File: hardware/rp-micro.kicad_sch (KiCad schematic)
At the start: 43 parts, among them J1 USB_C_Receptacle_USB2.0, J2 Conn_01x12, J3 Conn_01x12, J4 Conn_01x05, SW1 BOOT, SW2 RESET, U1 RT9013-33GB, U2 W25Q64JVXGIQ, U3 RP2040, Y1 12MHz

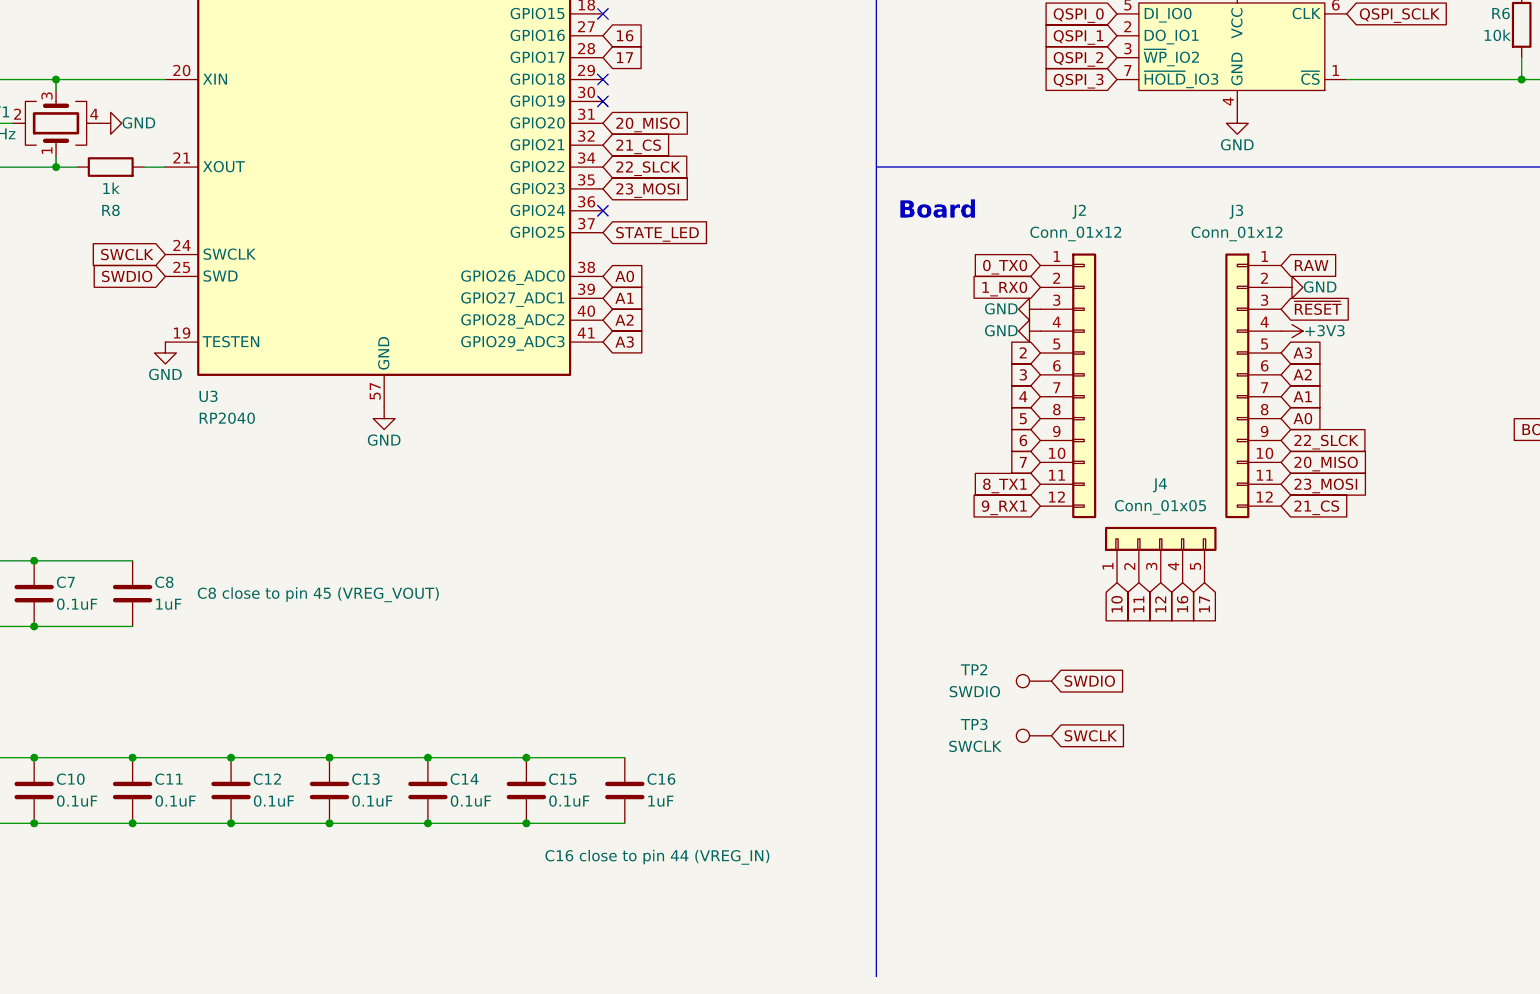
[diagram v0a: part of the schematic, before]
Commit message: Fix the typo
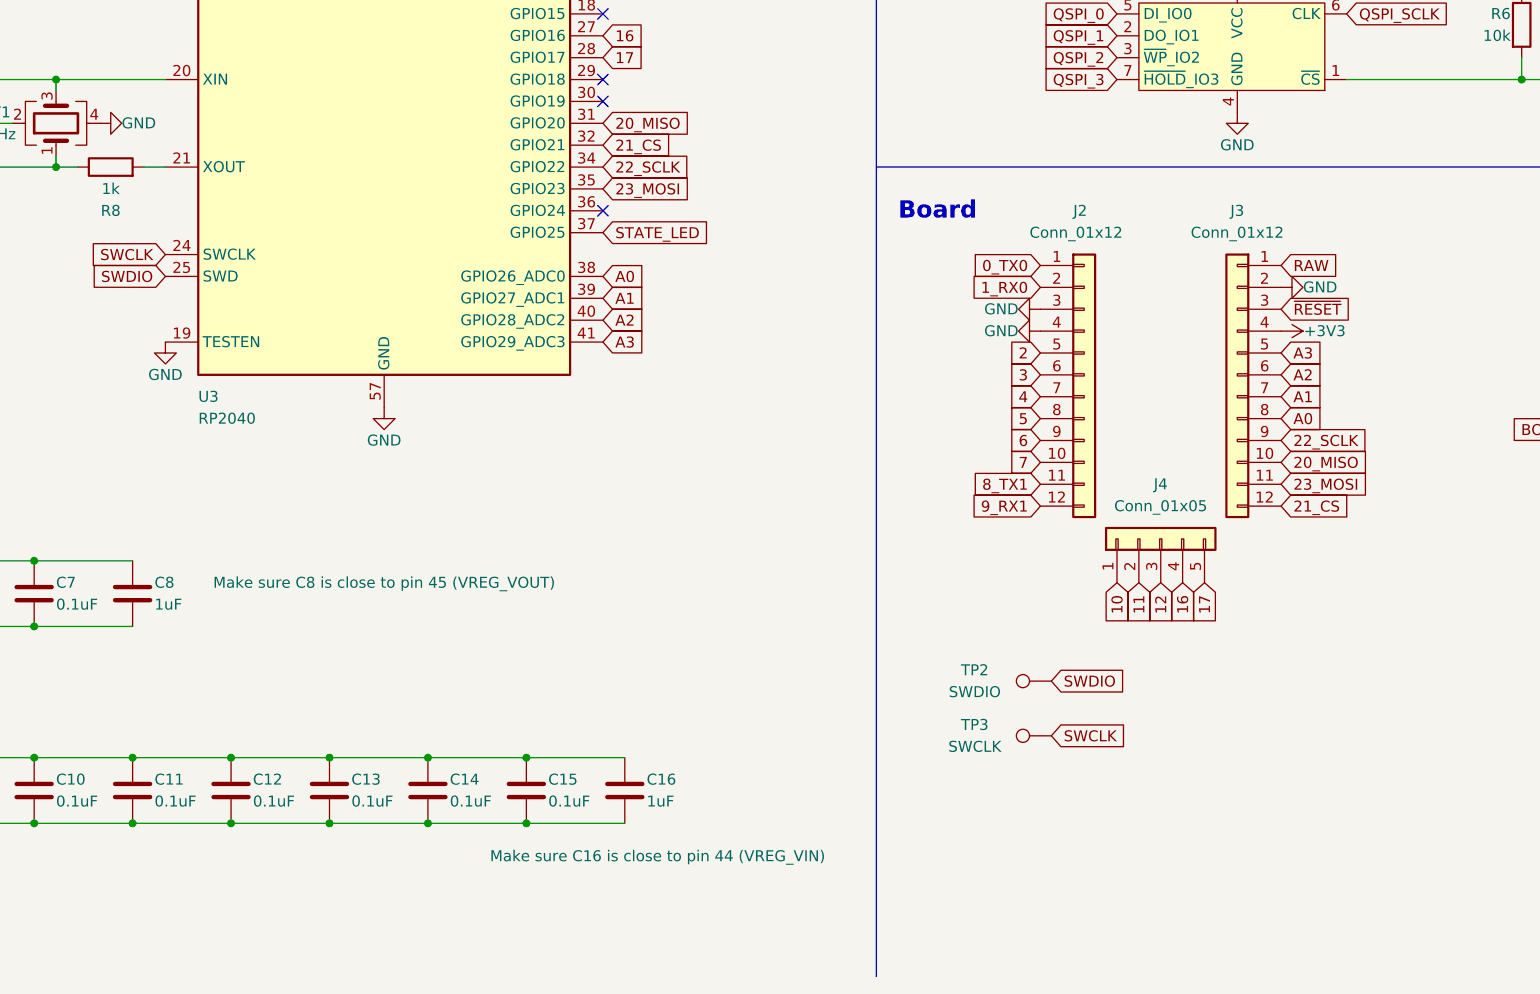
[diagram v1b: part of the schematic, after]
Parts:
- C16: Note ${REFERENCE} close to pin 44 (VREG_IN) -> Make sure ${REFERENCE} is close to pin 44 (VREG_VIN)
- C8: Note ${REFERENCE} close to pin 45 (VREG_VOUT) -> Make sure ${REFERENCE} is close to pin 45 (VREG_VOUT)
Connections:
- net 22_SLCK renamed 22_SCLK
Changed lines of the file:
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@@
   (title_block
     (title "RP Micro")
-    (date "2022-11-07")
+    (date "2022-11-13")
     (rev "1.0")
     (comment 1 "MIT License (Open source hardware)")
@@
     )
   )
-  (global_label "22_SLCK" (shape input) (at 107.95 104.14 0) (fields_autoplaced)
+  (global_label "22_SCLK" (shape input) (at 107.95 104.14 0) (fields_autoplaced)
     (effects (font (size 1.27 1.27)) (justify left))
     (property "Intersheet References" "${INTERSHEET_REFS}" (id 0) (at 118.5274 104.0606 0)
@@
     )
   )
-  (global_label "22_SLCK" (shape input) (at 186.69 135.89 0) (fields_autoplaced)
+  (global_label "22_SCLK" (shape input) (at 186.69 135.89 0) (fields_autoplaced)
     (effects (font (size 1.27 1.27)) (justify left))
     (property "Intersheet References" "${INTERSHEET_REFS}" (id 0) (at 197.2674 135.8106 0)
@@
       (effects (font (size 1.27 1.27)) hide)
     )
-    (property "Note" "${REFERENCE} close to pin 44 (VREG_IN)" (id 6) (at 114.3 184.15 0))
+    (property "Note" "Make sure ${REFERENCE} is close to pin 44 (VREG_VIN)" (id 6) (at 114.3 184.15 0))
     (pin "1")
     (pin "2")
@@
       (effects (font (size 1.27 1.27)) hide)
     )
-    (property "Note" "${REFERENCE} close to pin 45 (VREG_VOUT)" (id 6) (at 74.93 153.67 0))
-    (pin "1")
-    (pin "2")
+    (property "Note" "Make sure ${REFERENCE} is close to pin 45 (VREG_VOUT)" (id 6) (at 82.55 152.4 0))
+    (pin "1")
+    (pin "2")

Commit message: rev 1.1 completed
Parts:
- removed LD1: RED, LED_SMD:LED_0603_1608Metric, symbol Device:LED
- removed R3: 330, Resistor_SMD:R_0402_1005Metric, symbol Device:R
- added JP1, JP2: SolderJumper_3_Bridged12, Jumper:SolderJumper-3_P1.3mm_Bridged12_Pad1.0x1.5mm, symbol Jumper:SolderJumper_3_Bridged12
- J1: footprint rp-micro:USB_C_Receptacle_TYPE-C-31-M-12 -> rp-micro:USB Type-C Mid-Mount Receptacle 16P; JLCPCB Part # C165948 -> C223906; MFR. Part # TYPE-C-31-M-12 -> TYPE-C-31-M-13
- TP1: renamed from TP2; footprint TestPoint:TestPoint_Pad_D1.0mm -> TestPoint:TestPoint_Pad_D2.0mm
- TP2: renamed from TP3; footprint TestPoint:TestPoint_Pad_D1.0mm -> TestPoint:TestPoint_Pad_D2.0mm
- U2: JLCPCB Part # C2940195 -> (none); MFR. Part # W25Q64JVXGIQ -> (none)
- renumbered C6 to C1, C13 to C10, C14 to C11, C15 to C12, C16 to C13, C1 to C14, C2 to C15, C3 to C16, C9 to C2, C4 to C3, C5 to C4, C7 to C5, C10 to C6, C8 to C7, C11 to C8, C12 to C9, J4 to J3, J3 to J4, LD2 to LD1, R4 to R1, R5 to R2, R8 to R3, R7 to R4, R6 to R5, R1 to R6, R2 to R7, R9 to R8, R10 to R9, TP1 to TP3, U3 to U1, U1 to U3
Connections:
- net 10: now also JP1.3 (B); no longer J3.1 (Pin_1)
- net 11: now also JP2.3 (B); no longer J3.2 (Pin_2)
- net 12: now also J3.1 (Pin_1); no longer J3.3 (Pin_3)
- net GND: now also R9.2, JP1.1 (A), JP2.1 (A); no longer J2.3 (Pin_3), J2.4 (Pin_4), LD1.1 (K)
- net STATE_LED: now also LD1.2 (A); no longer R9.1
- net VBUS: now also F1.1, J1.A4 (VBUS), J1.A9 (VBUS), J1.B4 (VBUS), J1.B9 (VBUS); no longer D1.2 (A), F1.2
- net 13: now reaches U1.16 (GPIO13)
- net 13: now also J3.2 (Pin_2)
- net 14: now reaches U1.17 (GPIO14)
- net 14: now also J3.3 (Pin_3)
- net RPD-: now reaches R2.2, U1.46 (USB_DM)
- net RPD+: now reaches R1.2, U1.47 (USB_DP)
- net QSPI_0 renamed QSPI_D0
- net QSPI_1 renamed QSPI_D1
- net QSPI_2 renamed QSPI_D2
- net QSPI_3 renamed QSPI_D3
- new net: LD1.1 (K), R9.1
- new net: J2.4 (Pin_4), JP2.2 (C)
- new net: J2.3 (Pin_3), JP1.2 (C)
- new net +5V: D1.2 (A), F1.2
- no-connect marks 8 -> 6
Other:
- moved on the sheet: C16, F1, J1, J2, J3, J4, R1, R2, R4, R5, R6, R7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

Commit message: Update PCBA files
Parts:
- C1, C10, C11, C12, C2, C5, C6, C8, C9: value 0.1uF -> 100nF
- C15: renamed from C16; value 0.1uF -> 100nF
- J1: JLCPCB Part # C223906 -> C168688; MFR. Part # TYPE-C-31-M-13 -> 918-418K2024S40000
- SB1: renamed from JP1; now left out of the parts list
- SB2: renamed from JP2; now left out of the parts list
- U2: JLCPCB Part # (none) -> C2940195; MFR. Part # (none) -> W25Q64JVXGIQ
- renumbered C15 to C16, TP3 to TP1, TP1 to TP2, TP2 to TP3
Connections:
- net SB2_OUT: now reaches J2.4 (Pin_4), SB2.2 (C)
- net SB1_OUT: now reaches J2.3 (Pin_3), SB1.2 (C)
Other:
- moved on the sheet: C14, C16, D1, J2, J3, J4, LD1, R8, R9, SB1, SB2, SW1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

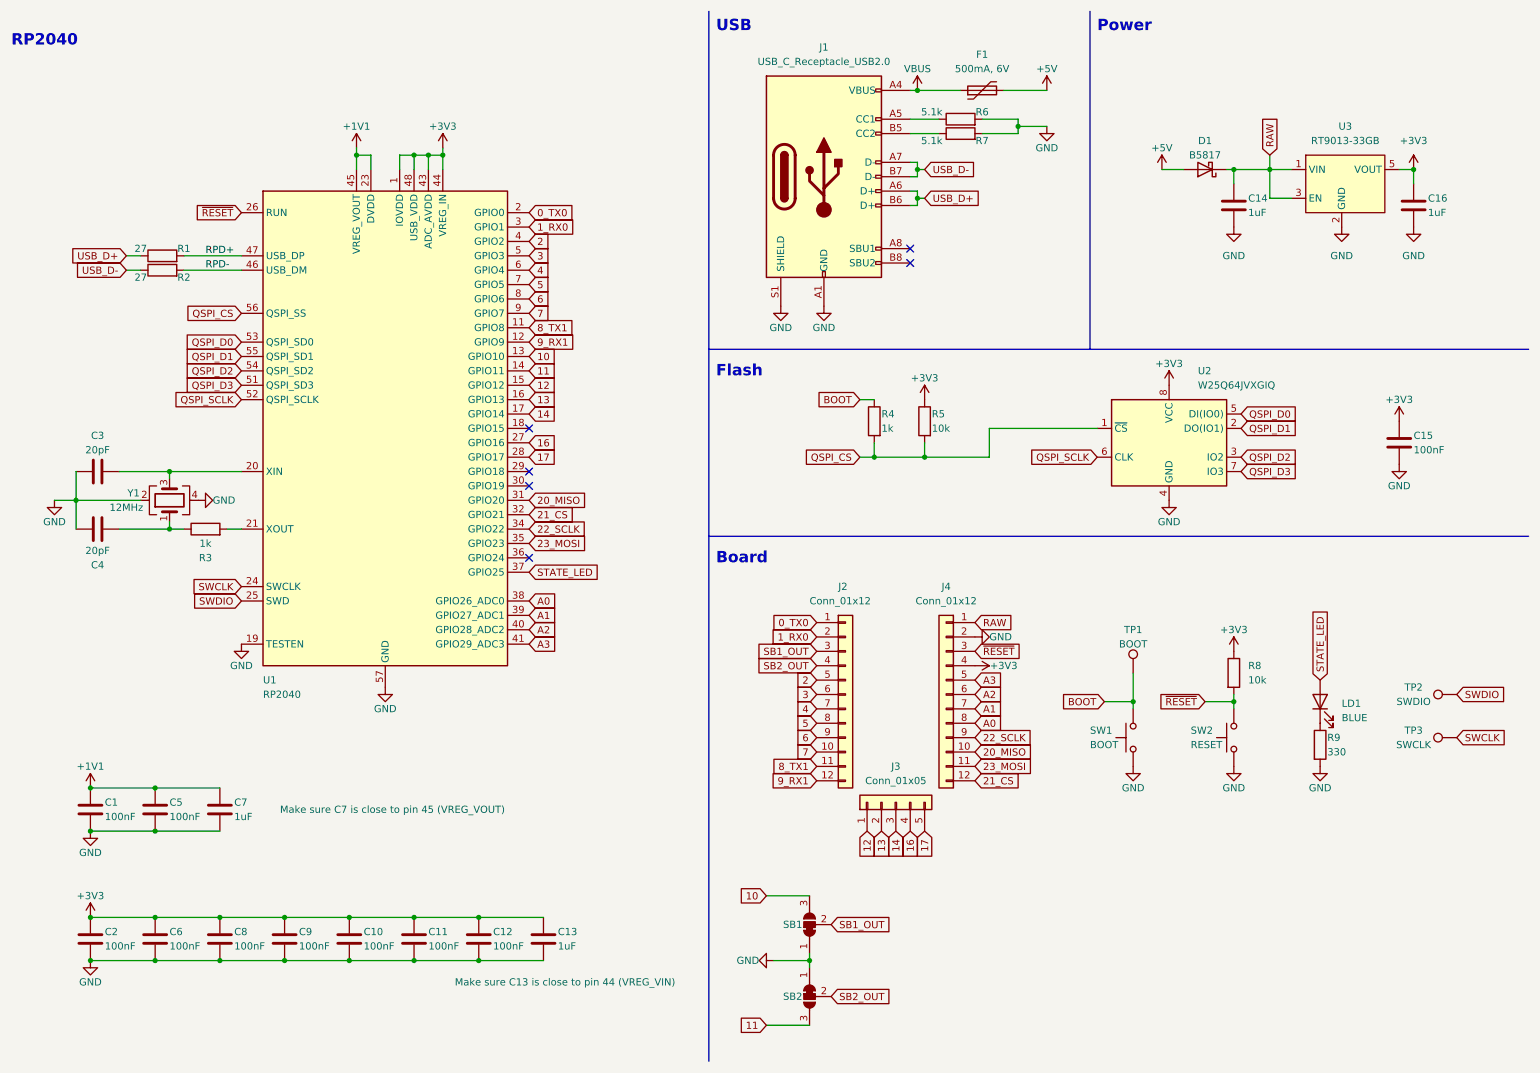
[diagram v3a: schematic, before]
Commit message: Change D1 footprint to hand soldering version
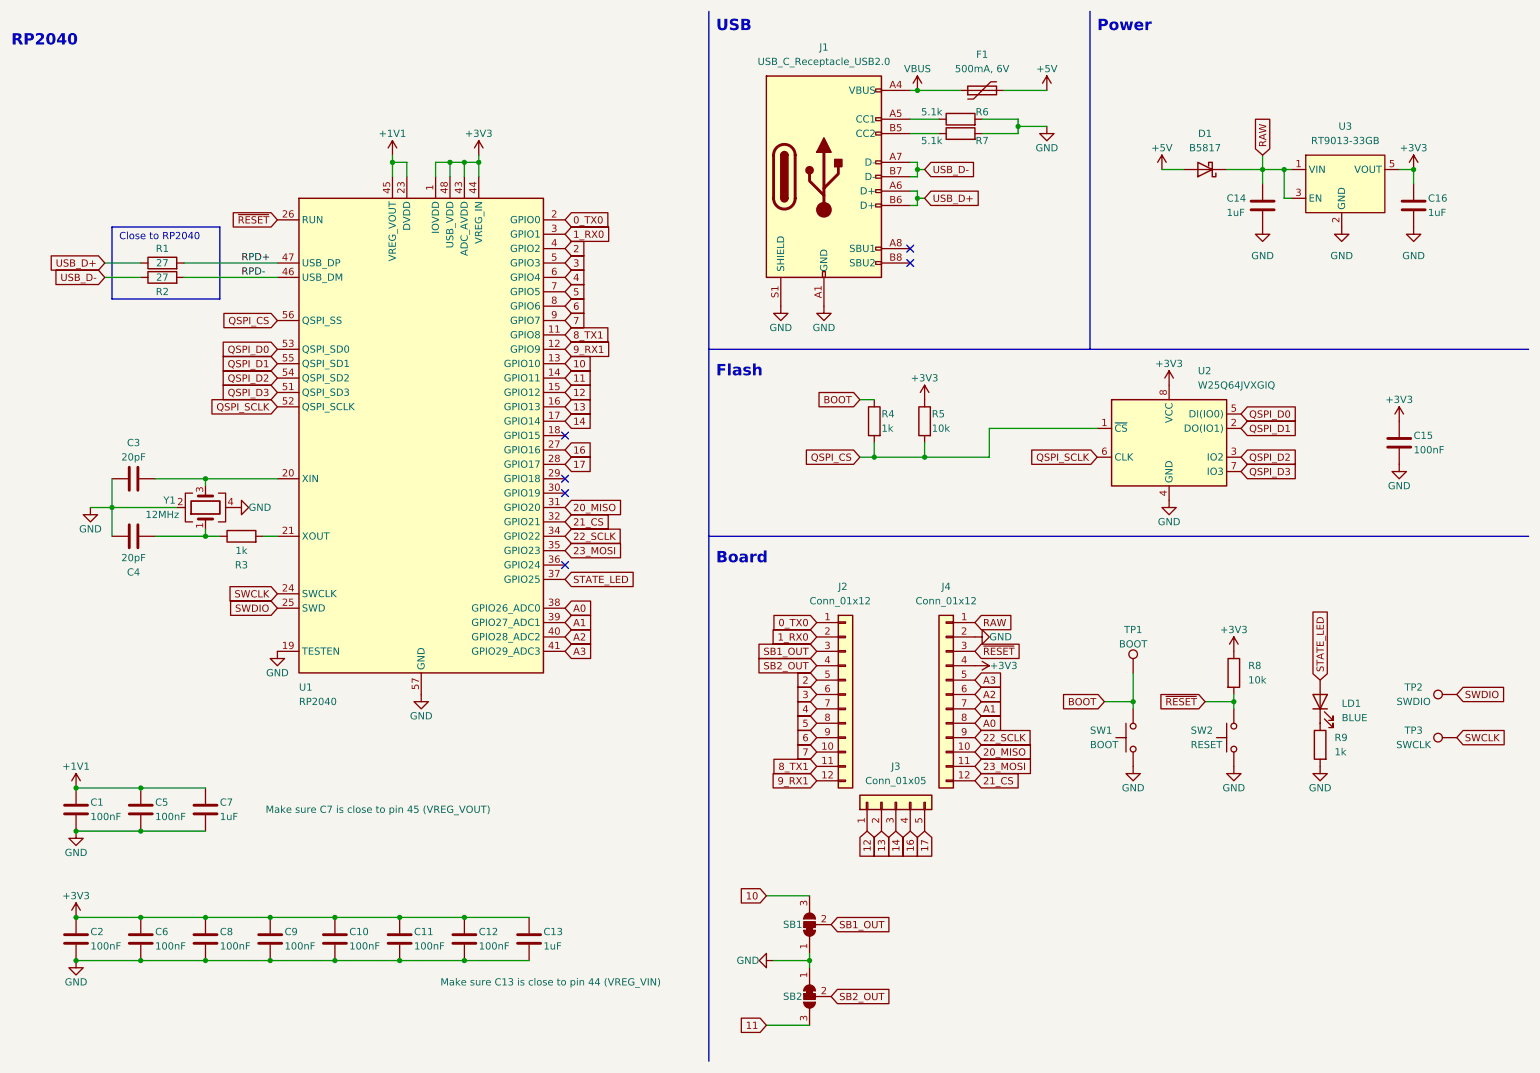
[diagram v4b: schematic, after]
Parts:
- D1: footprint Diode_SMD:D_SOD-323 -> Diode_SMD:D_SOD-323_HandSoldering
- R9: value 330 -> 1k; JLCPCB Part # C25104 -> C11702; MFR. Part # 0402WGF3300TCE -> 0402WGF1001TCE
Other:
- note added: "Close to RP2040"
- moved on the sheet: C1, C10, C11, C12, C13, C14, C2, C3, C4, C5, C6, C7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
